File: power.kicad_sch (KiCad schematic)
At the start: 41 parts, among them U1701 MC7805

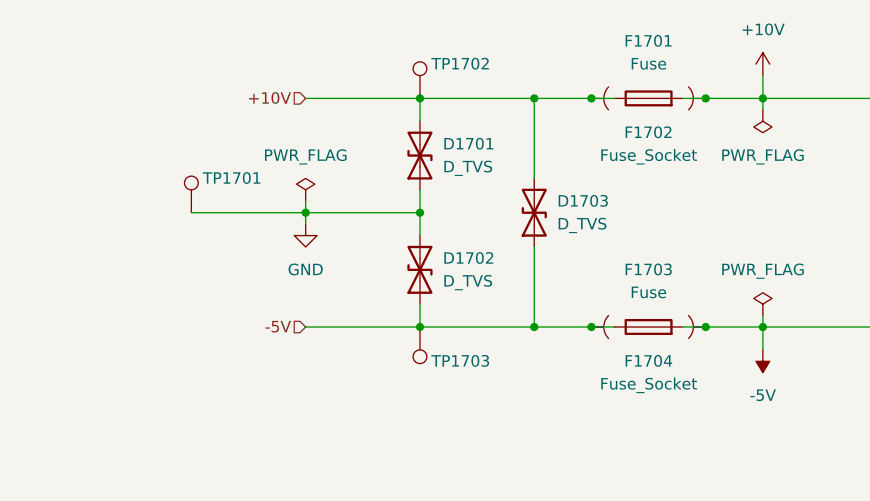
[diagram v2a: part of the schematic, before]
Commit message: fix schematic netlist error, two nets with same name
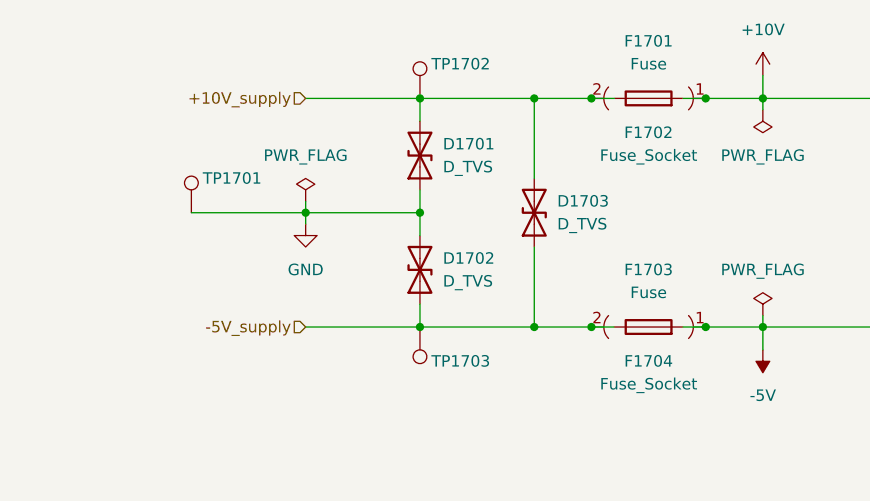
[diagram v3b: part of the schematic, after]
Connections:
- net +10V: no longer D1701.2 (A2), D1703.2 (A2), F1701.1, F1702.2, TP1702.1
- net -5V: no longer D1702.1 (A1), D1703.1 (A1), F1703.1, F1704.2, TP1703.1
- new net +10V_supply: D1701.2 (A2), D1703.2 (A2), F1701.1, F1702.2, TP1702.1
- new net -5V_supply: D1702.1 (A1), D1703.1 (A1), F1703.1, F1704.2, TP1703.1
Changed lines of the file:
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@@
 		(title "Power Supply Sink")
 		(date "2024-12-08")
-		(rev "0.13.5")
+		(rev "0.13.6")
 		(company "Open Battery Tester")
 		(comment 1 "Power")
@@
 		)
 	)
-	(hierarchical_label "-5V"
+	(hierarchical_label "-5V_supply"
 		(shape input)
 		(at 63.5 76.2 180)
@@
 		)
 	)
-	(hierarchical_label "+10V"
+	(hierarchical_label "+10V_supply"
 		(shape input)
 		(at 63.5 50.8 180)
@@
 	)
 	(symbol
+		(lib_name "Fuse_Socket_1")
 		(lib_id "pss:Fuse_Socket")
 		(at 101.6 50.8 270)

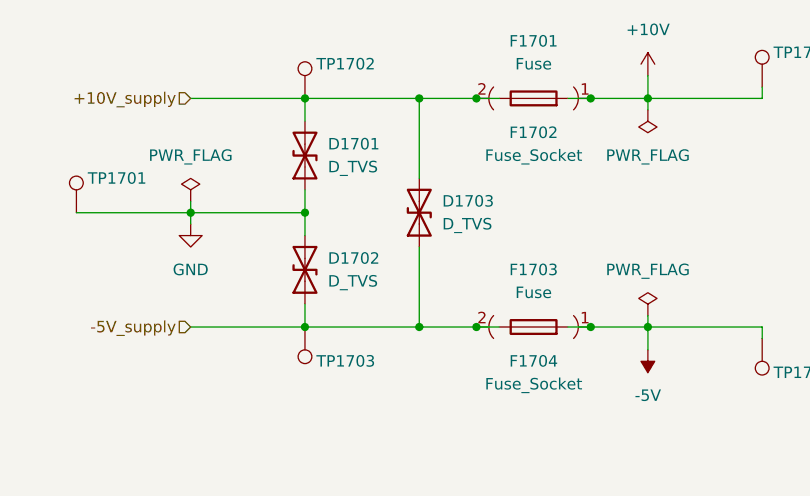
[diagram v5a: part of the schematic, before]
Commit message: remove power redundant esd protection diode
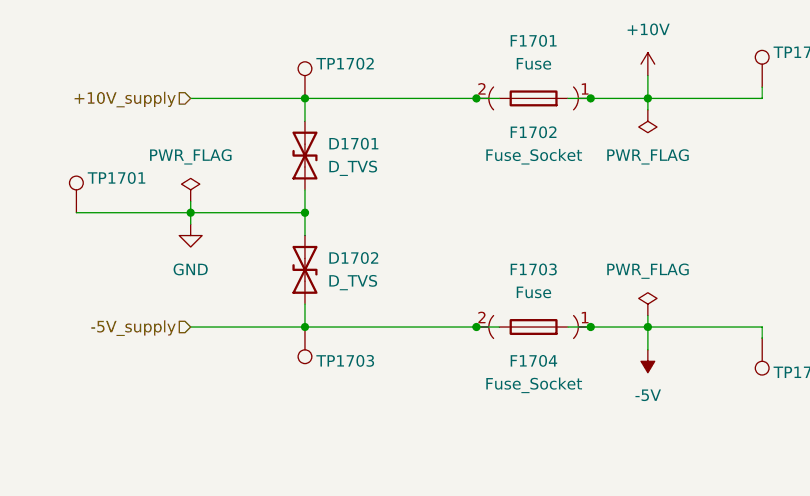
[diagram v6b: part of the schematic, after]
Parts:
- removed D1703: D_TVS, pss:D_SOD-323_HandSoldering, symbol pss:D_TVS
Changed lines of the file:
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@@
 	)
 	(junction
-		(at 88.9 50.8)
-		(diameter 0)
-		(color 0 0 0 0)
-	)
-	(junction
 		(at 95.25 50.8)
 		(diameter 0)
@@
 	)
 	(junction
-		(at 88.9 76.2)
-		(diameter 0)
-		(color 0 0 0 0)
-	)
-	(junction
 		(at 76.2 63.5)
 		(diameter 0)
@@
 	(wire
 		(pts
-			(xy 88.9 50.8) (xy 95.25 50.8)
+			(xy 76.2 50.8) (xy 95.25 50.8)
 		)
 		(stroke
@@
 	(wire
 		(pts
-			(xy 88.9 59.69) (xy 88.9 50.8)
-		)
-		(stroke
-			(width 0)
-			(type default)
-		)
-	)
-	(wire
-		(pts
 			(xy 48.26 167.64) (xy 54.61 167.64)
 		)
@@
 	(wire
 		(pts
-			(xy 88.9 76.2) (xy 95.25 76.2)
-		)
-		(stroke
-			(width 0)
-			(type default)
-		)
-	)
-	(wire
-		(pts
 			(xy 114.3 48.26) (xy 114.3 50.8)
 		)
@@
 	(wire
 		(pts
-			(xy 76.2 76.2) (xy 88.9 76.2)
+			(xy 76.2 76.2) (xy 95.25 76.2)
 		)
 		(stroke
@@
 	(wire
 		(pts
-			(xy 88.9 76.2) (xy 88.9 67.31)
-		)
-		(stroke
-			(width 0)
-			(type default)
-		)
-	)
-	(wire
-		(pts
 			(xy 127 160.02) (xy 128.27 160.02)
 		)
@@
 	(wire
 		(pts
-			(xy 88.9 50.8) (xy 76.2 50.8)
-		)
-		(stroke
-			(width 0)
-			(type default)
-		)
-	)
-	(wire
-		(pts
 			(xy 172.72 63.5) (xy 176.53 63.5)
 		)
@@
 					(unit 1)
 				)
-			)
-		)
-	)
-	(symbol
-		(lib_id "pss:D_TVS")
-		(at 88.9 63.5 90)
-		(unit 1)
-		(exclude_from_sim no)
-		(in_bom yes)
-		(on_board yes)
-		(dnp no)
-		(fields_autoplaced yes)
-		(property "Reference" "D1703"
-			(at 91.44 62.2299 90)
-			(effects
-				(font
-					(size 1.27 1.27)
-				)
-				(justify right)
-			)
-		)
-		(property "Value" "D_TVS"
-			(at 91.44 64.7699 90)
-			(effects
-				(font
-					(size 1.27 1.27)
-				)
-				(justify right)
-			)
-		)
-		(property "Footprint" "pss:D_SOD-323_HandSoldering"
-			(at 88.9 63.5 0)
-			(effects
-				(font
-					(size 1.27 1.27)
-				)
-				(hide yes)
-			)
-		)
-		(property "Datasheet" "./datasheet/UDD32C15L01.pdf"
-			(at 88.9 63.5 0)
-			(effects
-				(font
-					(size 1.27 1.27)
-				)
-				(hide yes)
-			)
-		)
-		(property "Description" "Bidirectional transient-voltage-suppression diode"
-			(at 88.9 63.5 0)
-			(effects
-				(font
-					(size 1.27 1.27)
-				)
-				(hide yes)
-			)
-		)
-		(property "MPN" "UDD32C15L01"
-			(at 88.9 63.5 0)
-			(effects
-				(font
-					(size 1.27 1.27)
-				)
-				(hide yes)
-			)
-		)
-		(property "VPN" "603-UDD32C15L01"
-			(at 88.9 63.5 0)
-			(effects
-				(font
-					(size 1.27 1.27)
-				)
-				(hide yes)
-			)
-		)
-		(pin "1"
-		)
-		(pin "2"
-		)
-		(instances
-			(project "pss"
-				(path "/3c438cf7-9350-4e9f-8115-1deba8984176/f49135f8-6951-492d-90df-5960b4866d04"
-					(reference "D1703")
-					(unit 1)
-				)
